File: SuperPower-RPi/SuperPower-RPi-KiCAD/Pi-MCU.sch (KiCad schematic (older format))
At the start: 36 parts, among them J10 Conn_01x04, J11 QWIIC_Connector, J12 DNP, J5 Conn_01x06, J7 Conn_01x03, J8 Conn_02x05_Odd_Even, J9 Conn_01x02, SW1 Tact, U3 STM32F412RETx, U4 ATtiny85-20SU, U5 ME6210A33M3G

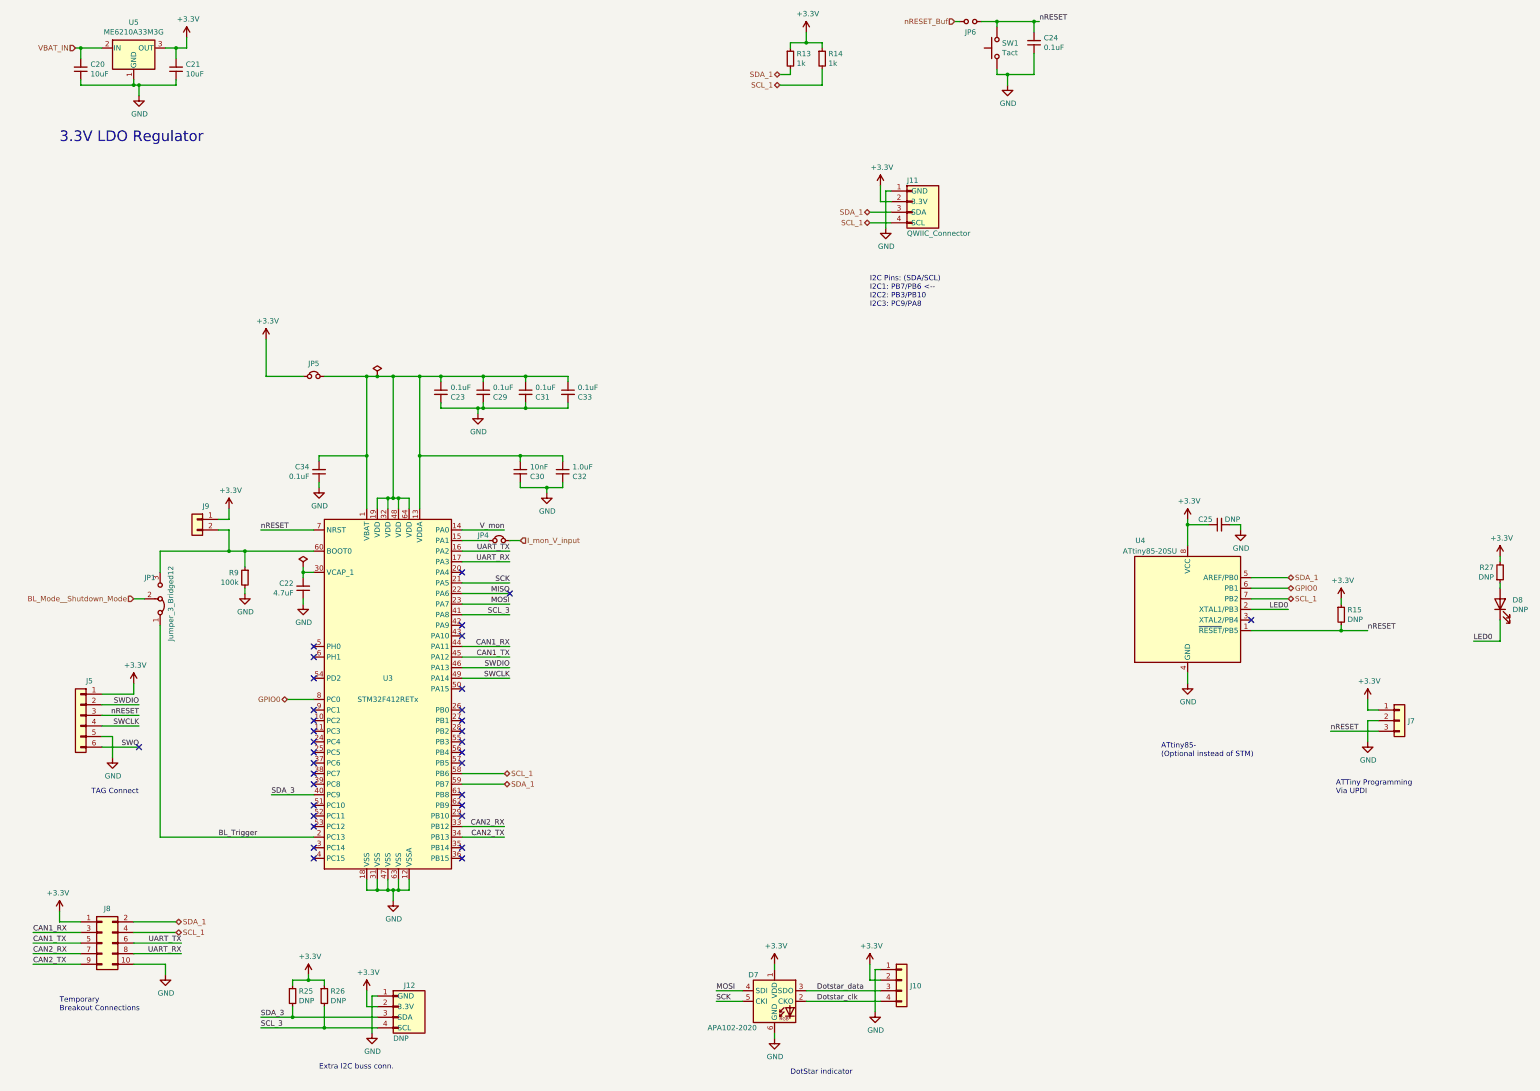
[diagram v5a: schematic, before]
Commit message: Updated MCU page to add a couple connections and move the LDO.
Moved the 3.3V LDO over to the Boost converter page.  Additionally, a
5V global node was made to facilitate the SPI connector jumper.
This 5V global node is only for incidental consumers of the power.
The primary power path is still maintained across the center of the
top schematic sheet.

An SPI connector was added to allow people to add SPI devices as
needed.
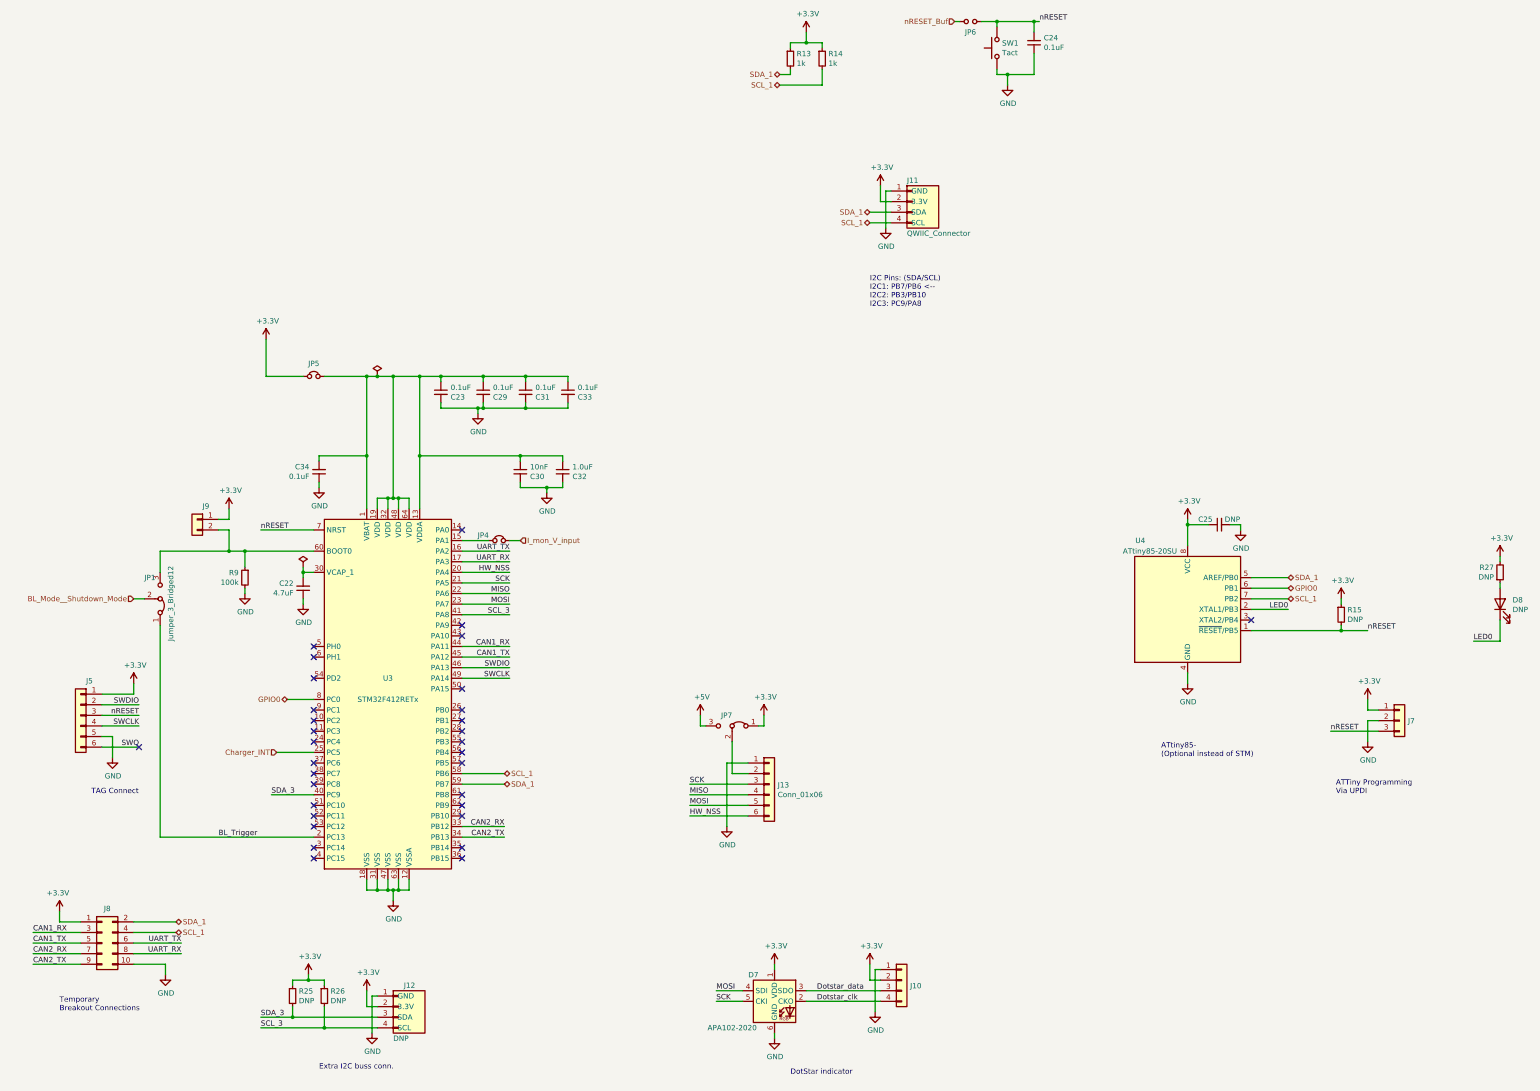
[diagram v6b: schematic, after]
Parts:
- removed C20, C21: 10uF, Capacitor_SMD:C_0805_2012Metric, symbol Device:C_Small
- removed U5: ME6210A33M3G, Package_TO_SOT_SMD:SOT-23, symbol Manual_Lib:ME6210A33M3G
- added J13: Conn_01x06, Connector_PinHeader_2.54mm:PinHeader_1x06_P2.54mm_Vertical, symbol Connector_Generic:Conn_01x06
- added JP7: Jumper_3_Bridged12, Jumper:SolderJumper-3_P1.3mm_Bridged12_RoundedPad1.0x1.5mm_NumberLabels, symbol Jumper:Jumper_3_Bridged12
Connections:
- net +3V3: now also JP7.1 (A)
- net GND: now also J13.1 (Pin_1)
- net MISO: now also J13.4 (Pin_4)
- net MOSI: now also J13.5 (Pin_5)
- net SCK: now also J13.3 (Pin_3)
- net HW_NSS: now reaches U3.20 (PA4)
- net HW_NSS: now also J13.6 (Pin_6)
- net Charger_INT: now reaches U3.25 (PC5)
- net V_mon: no longer names the net of U3.14 (PA0)
- new net: J13.2 (Pin_2), JP7.2 (C)
- new net +5V: JP7.3 (B)
- no-connect marks 34 -> 32
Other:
- note removed: "3.3V LDO Regulator"
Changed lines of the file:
@@
 Connection ~ 10250 900
-Wire Wire Line
-	2050 1150 2150 1150
-Wire Wire Line
-	2150 1150 2150 1250
-$Comp
-L power:GND #PWR020
-U 1 1 5FA628B7
-P 1800 1600
-F 0 "#PWR020" H 1800 1350 50  0001 C CNN
-F 1 "GND" H 1805 1427 50  0000 C CNN
-F 2 "" H 1800 1600 50  0001 C CNN
-F 3 "" H 1800 1600 50  0001 C CNN
-	1    1800 1600
-	1    0    0    -1
-$EndComp
-Wire Wire Line
-	1800 1600 1800 1500
-Wire Wire Line
-	1750 1500 1800 1500
-Wire Wire Line
-	2150 1500 2150 1450
-Wire Wire Line
-	1750 1500 1750 1450
-Connection ~ 1800 1500
-Wire Wire Line
-	1800 1500 2150 1500
-Wire Wire Line
-	1750 1500 1250 1500
-Wire Wire Line
-	1250 1500 1250 1450
-Connection ~ 1750 1500
-Wire Wire Line
-	1250 1250 1250 1150
-Wire Wire Line
-	1250 1150 1450 1150
-Wire Wire Line
-	1250 1150 1200 1150
-Connection ~ 1250 1150
-Text HLabel 1200 1150 0    50   Input ~ 0
-VBAT_IN
 Wire Wire Line
 	4350 9100 4250 9100
@@
 NoConn ~ 3450 8000
 NoConn ~ 3450 7900
-NoConn ~ 3450 7800
 NoConn ~ 3450 7700
 NoConn ~ 3450 7600
@@
 NoConn ~ 4850 6700
 NoConn ~ 4850 6600
-NoConn ~ 4850 6100
 $Comp
 L power:GND #PWR021
@@
 	1    0    0    -1
 $EndComp
-$Comp
-L power:+3.3V #PWR016
-U 1 1 5FB90BA7
-P 2250 1050
-F 0 "#PWR016" H 2250 900 50  0001 C CNN
-F 1 "+3.3V" H 2265 1223 50  0000 C CNN
-F 2 "" H 2250 1050 50  0001 C CNN
-F 3 "" H 2250 1050 50  0001 C CNN
-	1    2250 1050
-	1    0    0    -1
-$EndComp
-Connection ~ 2150 1150
-Text Label 5250 5700 2    50   ~ 0
-V_mon
 Wire Wire Line
 	4450 5000 5400 5000
-Wire Wire Line
-	4850 5700 5250 5700
-Wire Wire Line
-	2250 1150 2250 1050
-Wire Wire Line
-	2150 1150 2250 1150
 Wire Wire Line
 	3950 5000 3500 5000
@@
 Text Label 8200 10150 0    50   ~ 0
 Dotstar_clk
-NoConn ~ 5300 6300
 Wire Wire Line
 	4850 8100 5250 8100
@@
 Wire Wire Line
 	4050 4250 4200 4250
-Text Notes 1050 2050 0    100  ~ 0
-3.3V LDO Regulator
 Wire Wire Line
 	4850 5900 5300 5900
@@
 $EndComp
 $Comp
-L Manual_Lib:ME6210A33M3G U5
-U 1 1 5FA5D721
-P 1750 1150
-F 0 "U5" H 1750 1392 50  0000 C CNN
-F 1 "ME6210A33M3G" H 1750 1301 50  0000 C CNN
-F 2 "Package_TO_SOT_SMD:SOT-23" H 2200 900 50  0001 L CIN
-F 3 "https://datasheet.lcsc.com/szlcsc/1810201611_MICRONE-Nanjing-Micro-One-Elec-ME6210A33PG_C85233.pdf" H 1750 1100 50  0001 C CNN
-F 4 "MicrOne" H 2350 750 50  0001 C CNN "Mfg"
-F 5 "ME6210A33M3G" H 2500 800 50  0001 C CNN "Mfg PN"
-	1    1750 1150
-	1    0    0    -1
-$EndComp
-$Comp
-L Device:C_Small C21
-U 1 1 5FA5DD96
-P 2150 1350
-F 0 "C21" H 2058 1304 50  0000 R CNN
-F 1 "10uF" H 2058 1395 50  0000 R CNN
-F 2 "Capacitor_SMD:C_0805_2012Metric" H 2150 1350 50  0001 C CNN
-F 3 "~" H 2150 1350 50  0001 C CNN
-F 4 "490-5523-1-ND" H 2150 1350 50  0001 C CNN "Digi-Key PN"
-F 5 "Murata" H 2150 1350 50  0001 C CNN "Mfg"
-F 6 "GRM21BR61E106KA73L" H 2150 1350 50  0001 C CNN "Mfg PN"
-	1    2150 1350
-	-1   0    0    1
-$EndComp
-$Comp
-L Device:C_Small C20
-U 1 1 5FA5E248
-P 1250 1350
-F 0 "C20" H 1158 1304 50  0000 R CNN
-F 1 "10uF" H 1158 1395 50  0000 R CNN
-F 2 "Capacitor_SMD:C_0805_2012Metric" H 1250 1350 50  0001 C CNN
-F 3 "~" H 1250 1350 50  0001 C CNN
-F 4 "490-5523-1-ND" H 1250 1350 50  0001 C CNN "Digi-Key PN"
-F 5 "Murata" H 1250 1350 50  0001 C CNN "Mfg"
-F 6 "GRM21BR61E106KA73L" H 1250 1350 50  0001 C CNN "Mfg PN"
-	1    1250 1350
-	-1   0    0    1
-$EndComp
-$Comp
 L Connector_Generic:Conn_01x03 J7
 U 1 1 5FA390FB
@@
 Text HLabel 1750 6350 0    50   Input ~ 0
 BL_Mode__Shutdown_Mode
+$Comp
+L Connector_Generic:Conn_01x06 J13
+U 1 1 5FD995FB
+P 7750 8100
+F 0 "J13" H 7830 8092 50  0000 L CNN
+F 1 "Conn_01x06" H 7830 8001 50  0000 L CNN
+F 2 "Connector_PinHeader_2.54mm:PinHeader_1x06_P2.54mm_Vertical" H 7750 8100 50  0001 C CNN
+F 3 "~" H 7750 8100 50  0001 C CNN
+	1    7750 8100
+	1    0    0    -1
+$EndComp
+$Comp
+L power:GND #PWR037
+U 1 1 5FD99B0C
+P 7350 8500
+F 0 "#PWR037" H 7350 8250 50  0001 C CNN
+F 1 "GND" H 7355 8327 50  0000 C CNN
+F 2 "" H 7350 8500 50  0001 C CNN
+F 3 "" H 7350 8500 50  0001 C CNN
+	1    7350 8500
+	1    0    0    -1
+$EndComp
+Wire Wire Line
+	7350 8500 7350 7900
+Wire Wire Line
+	7350 7900 7550 7900
+Text Label 7000 8100 0    50   ~ 0
+SCK
+Text Label 7000 8200 0    50   ~ 0
+MISO
+Text Label 7000 8300 0    50   ~ 0
+MOSI
+$Comp
+L power:+3.3V #PWR038
+U 1 1 5FDB1EAF
+P 7700 7450
+F 0 "#PWR038" H 7700 7300 50  0001 C CNN
+F 1 "+3.3V" H 7715 7623 50  0000 C CNN
+F 2 "" H 7700 7450 50  0001 C CNN
+F 3 "" H 7700 7450 50  0001 C CNN
+	1    7700 7450
+	1    0    0    -1
+$EndComp
+$Comp
+L Jumper:Jumper_3_Bridged12 JP7
+U 1 1 5FDB24E8
+P 7400 7550
+F 0 "JP7" H 7400 7650 50  0000 L CNN
+F 1 "Jumper_3_Bridged12" H 7000 7650 50  0001 L CNN
+F 2 "Jumper:SolderJumper-3_P1.3mm_Bridged12_RoundedPad1.0x1.5mm_NumberLabels" H 7400 7550 50  0001 C CNN
+F 3 "~" H 7400 7550 50  0001 C CNN
+	1    7400 7550
+	-1   0    0    -1
+$EndComp
+Wire Wire Line
+	7650 7550 7700 7550
+Wire Wire Line
+	7700 7550 7700 7450
+Wire Wire Line
+	7400 8000 7550 8000
+$Comp
+L power:+5V #PWR049
+U 1 1 5FE3F788
+P 7100 7450
+F 0 "#PWR049" H 7100 7300 50  0001 C CNN
+F 1 "+5V" H 7115 7623 50  0000 C CNN
+F 2 "" H 7100 7450 50  0001 C CNN
+F 3 "" H 7100 7450 50  0001 C CNN
+	1    7100 7450
+	1    0    0    -1
+$EndComp
+Wire Wire Line
+	7100 7450 7100 7550
+Wire Wire Line
+	7100 7550 7150 7550
+NoConn ~ 4850 5700
+Wire Wire Line
+	7550 8300 7000 8300
+Wire Wire Line
+	7000 8100 7550 8100
+Wire Wire Line
+	7000 8200 7550 8200
+Wire Wire Line
+	7550 8400 7000 8400
+Text HLabel 3100 7800 0    50   Input ~ 0
+Charger_INT
+Wire Wire Line
+	4850 6100 5300 6100
+Text Label 5300 6100 2    50   ~ 0
+HW_NSS
+Text Label 7000 8400 0    50   ~ 0
+HW_NSS
+Wire Wire Line
+	3100 7800 3450 7800
+Wire Wire Line
+	7400 7700 7400 8000
 $EndSCHEMATC

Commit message: Further PCB work with a net-label addition.
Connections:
- net 3.3V_MCU: now reaches C23.1, C29.1, C30.1, C31.1, C32.1, C33.1, C34.2, JP5.2, U3.1 (VBAT), U3.13 (VDDA), U3.19 (VDD), U3.32 (VDD), U3.48 (VDD), U3.64 (VDD)
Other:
- moved on the sheet: JP5
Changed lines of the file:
@@
 	14650 6000 14650 5950
 Wire Wire Line
-	3350 4250 3000 4250
-Wire Wire Line
-	3550 4250 3950 4250
+	3250 4250 3000 4250
+Wire Wire Line
+	3450 4250 3950 4250
 Connection ~ 3950 4250
 $Comp
@@
 L Device:Jumper_NC_Small JP5
 U 1 1 5FF2721E
-P 3450 4250
-F 0 "JP5" H 3450 4371 50  0000 C CNN
-F 1 "Jumper_NC_Small" H 3450 4371 50  0001 C CNN
-F 2 "SuperPower-RPi-KiCAD:PinHeader_1x02_P2.54mm_Vertical_Shorted" H 3450 4250 50  0001 C CNN
-F 3 "~" H 3450 4250 50  0001 C CNN
-F 4 "DNP" H 3450 4250 50  0001 C CNN "Mfg"
-	1    3450 4250
+P 3350 4250
+F 0 "JP5" H 3350 4371 50  0000 C CNN
+F 1 "Jumper_NC_Small" H 3350 4371 50  0001 C CNN
+F 2 "SuperPower-RPi-KiCAD:PinHeader_1x02_P2.54mm_Vertical_Shorted" H 3350 4250 50  0001 C CNN
+F 3 "~" H 3350 4250 50  0001 C CNN
+F 4 "DNP" H 3350 4250 50  0001 C CNN "Mfg"
+	1    3350 4250
 	1    0    0    -1
 $EndComp
@@
 Wire Wire Line
 	7400 7700 7400 8000
+Text Label 3550 4250 0    50   ~ 0
+3.3V_MCU
 $EndSCHEMATC

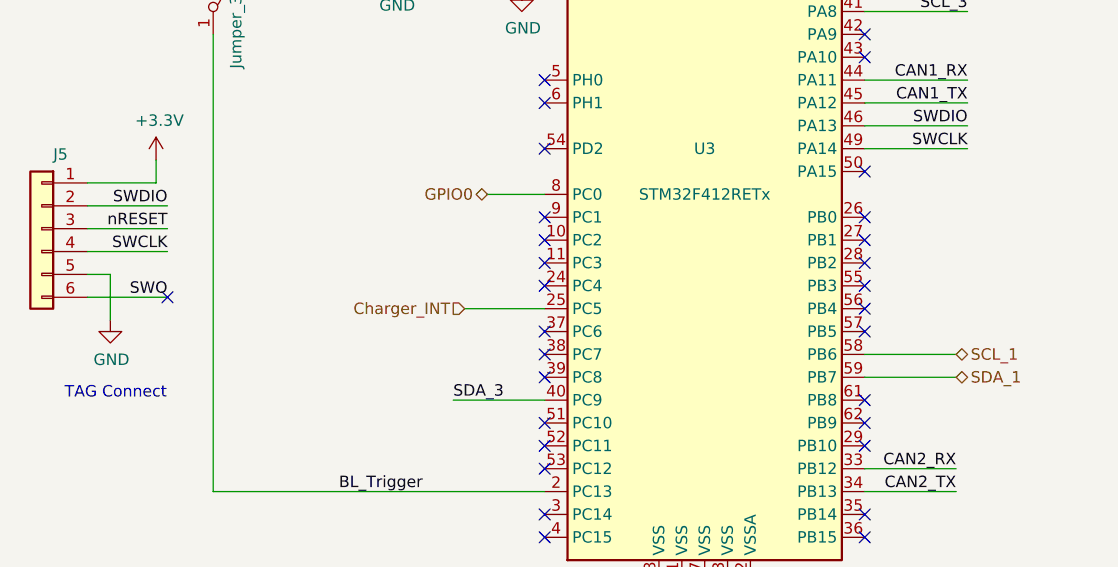
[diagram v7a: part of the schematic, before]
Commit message: Added SWO connector on MCU.
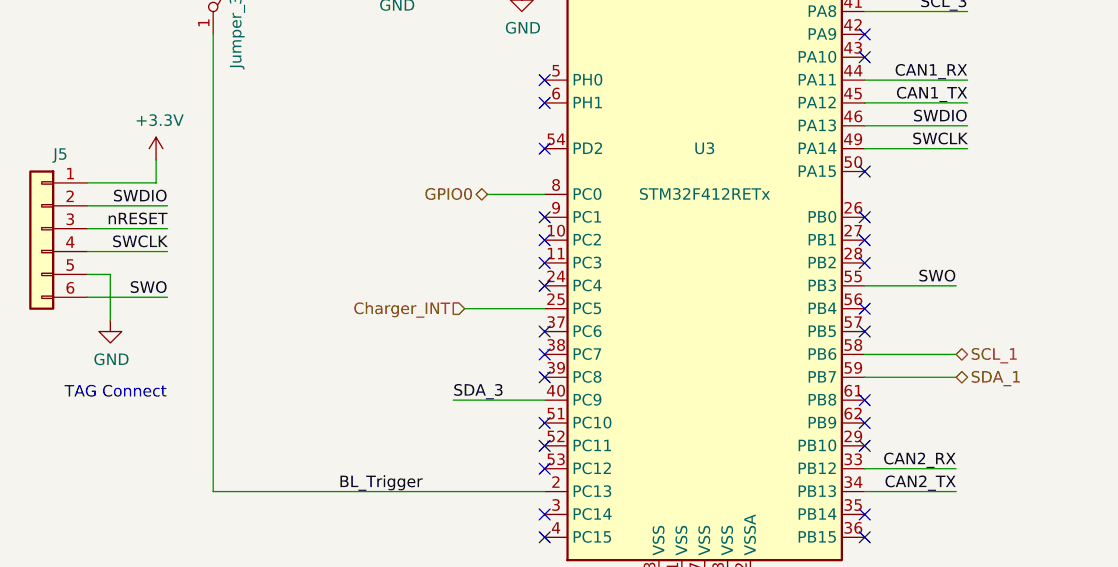
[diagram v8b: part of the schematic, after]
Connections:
- net SWO: now also U3.55 (PB3)
- no-connect marks 32 -> 30
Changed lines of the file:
@@
 Wire Wire Line
 	1550 7650 1550 7850
-Text Label 1800 7750 2    50   ~ 0
-SWO
 Wire Wire Line
 	1800 7750 1450 7750
@@
 NoConn ~ 4850 7500
 NoConn ~ 4850 7600
-NoConn ~ 4850 7700
 NoConn ~ 4850 7800
 NoConn ~ 4850 7900
@@
 Wire Wire Line
 	1050 9400 1250 9400
-NoConn ~ 1800 7750
 $Comp
 L power:PWR_FLAG #FLG0108
@@
 Text Label 3550 4250 0    50   ~ 0
 3.3V_MCU
+Wire Wire Line
+	4850 7700 5250 7700
+Text Label 5250 7700 2    50   ~ 0
+SWO
+Text Label 1800 7750 2    50   ~ 0
+SWO
 $EndSCHEMATC
